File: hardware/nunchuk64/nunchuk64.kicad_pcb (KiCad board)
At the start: 2 copper layers, 49.9 x 41.5 mm, 28 parts, among them J1 DB9_Female, J2 DB9_Female, J3 Conn_02x03_Odd_Even, P1 CONN_WII, P2 CONN_WII, Q1 BSS138, Q2 BSS138, Q3 BSS138, Q4 BSS138, SW1 SW_Push, U1 AMS1117-3V3, U2 ATMEGA328P-AU

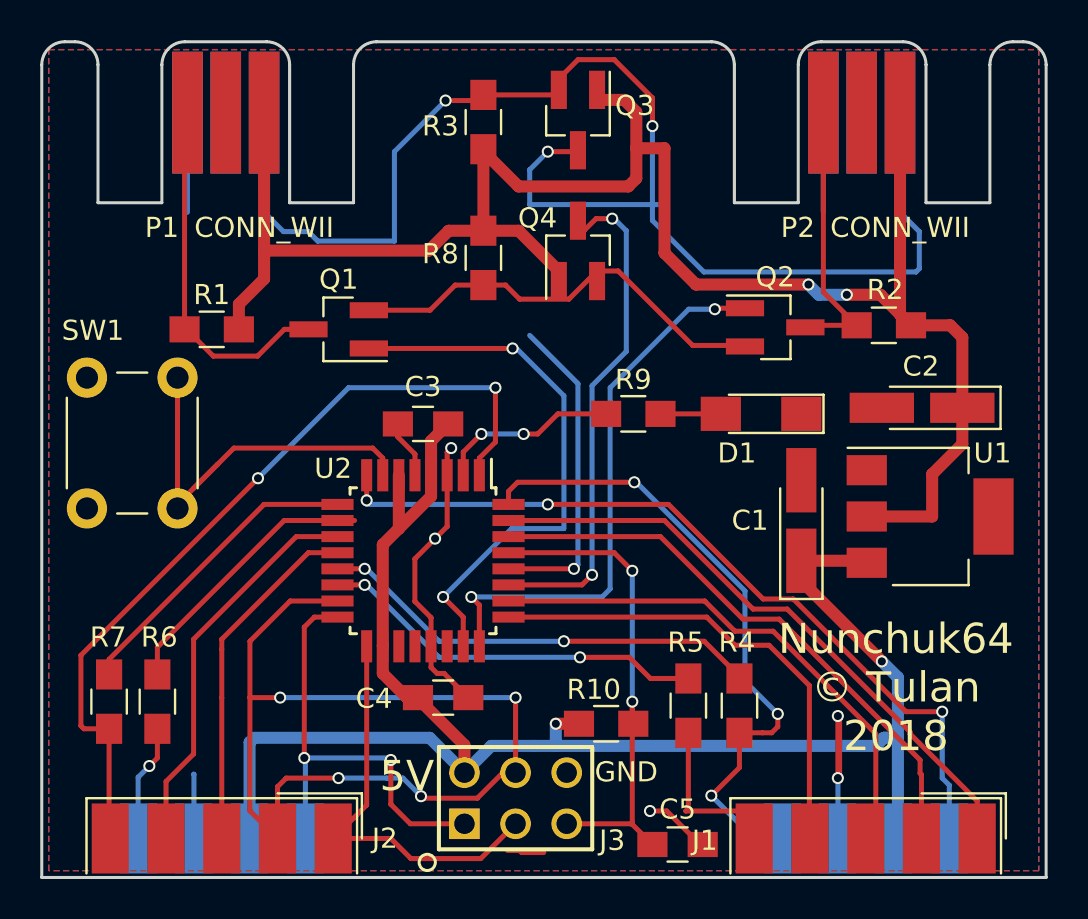
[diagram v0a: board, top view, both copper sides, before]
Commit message: fix: accidentally rotated a net. island gnd fill
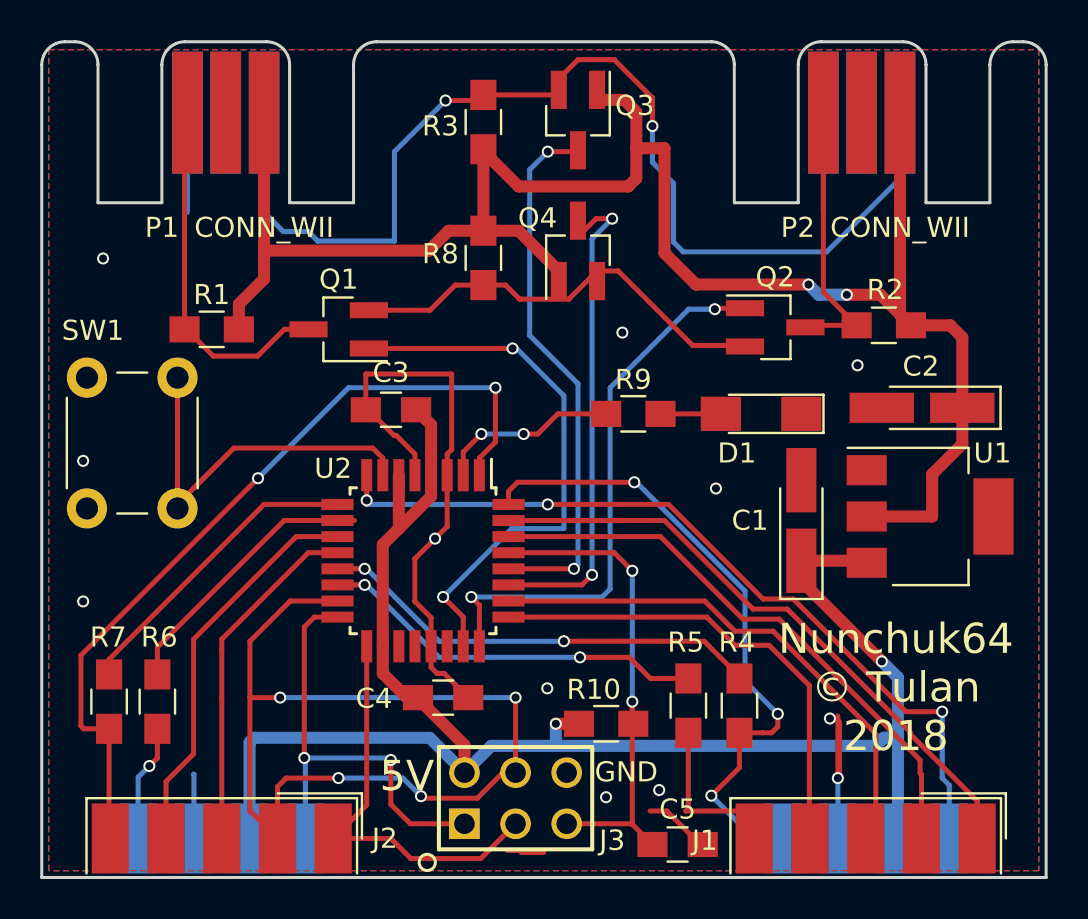
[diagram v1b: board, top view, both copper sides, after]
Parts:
- moved C3 1.74 mm to (93.8, 90.3)
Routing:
- net GND: track 42.9 -> 54.1 mm, vias 5 -> 2
- net /SCL: track 61.9 -> 57.1 mm
- net +5V: track 84.7 -> 85.4 mm
- net /SDA_: track 25.1 -> 24.4 mm
- net (no net): vias 0 -> 10

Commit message: DRC OK
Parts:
- moved C1 0.11 mm to (114.2, 95.7)
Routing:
- net GND: track 54.1 -> 112.5 mm, vias 2 -> 9
- net /SCL: track 57.1 -> 59.8 mm
- net /SDA: track 22.1 -> 22.7 mm
- net (no net): vias 10 -> 0
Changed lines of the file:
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@@
   (general
     (links 79)
-    (no_connects 2)
+    (no_connects 0)
     (area 69.224999 71.755 133.575001 129.535)
     (thickness 1.6)
     (drawings 38)
-    (tracks 412)
+    (tracks 440)
     (zones 0)
     (modules 28)
@@
     (tags "resistor 0805")
     (attr smd)
-    (fp_text reference R10 (at -0.614 -1.7) (layer F.SilkS)
-      (effects (font (size 1 1) (thickness 0.15)))
+    (fp_text reference R10 (at -0.614 -1.7) (layer B.SilkS)
+      (effects (font (size 1 1) (thickness 0.15)) (justify mirror))
     )
     (fp_text value 10k (at 0 1.75) (layer F.Fab)
@@
   )
   (module Capacitors_Tantalum_SMD:CP_Tantalum_Case-A_EIA-3216-18_Hand (layer F.Cu)
-    (at 114.2 95.8 90)
+    (at 114.1984 95.6884 90)
     (descr "Tantalum capacitor, Case A, EIA 3216-18, 3.2x1.6x1.6mm, Hand soldering footprint")
     (tags "capacitor tantalum smd")
@@
   (segment (start 100.2 112.2) (end 100.3 112.3) (width 0.25) (layer F.Cu) (net 0))
   (segment (start 99.6 112.2) (end 100.2 112.2) (width 0.25) (layer F.Cu) (net 0))
-  (via (at 101.5746 104.14) (size 0.6) (drill 0.4) (layers F.Cu B.Cu) (net 0))
-  (via (at 78.5114 99.822) (size 0.6) (drill 0.4) (layers F.Cu B.Cu) (net 0))
-  (via (at 78.5114 92.837) (size 0.6) (drill 0.4) (layers F.Cu B.Cu) (net 0))
-  (via (at 79.502 82.7786) (size 0.6) (drill 0.4) (layers F.Cu B.Cu) (net 0))
-  (via (at 104.4956 109.5502) (size 0.6) (drill 0.4) (layers F.Cu B.Cu) (net 0))
-  (via (at 116.9924 88.0872) (size 0.6) (drill 0.4) (layers F.Cu B.Cu) (net 0))
-  (via (at 109.9566 94.2086) (size 0.6) (drill 0.4) (layers F.Cu B.Cu) (net 0))
-  (via (at 105.3084 86.4616) (size 0.6) (drill 0.4) (layers F.Cu B.Cu) (net 0))
-  (via (at 107.1372 109.1946) (size 0.6) (drill 0.4) (layers F.Cu B.Cu) (net 0))
-  (via (at 115.6208 105.6386) (size 0.6) (drill 0.4) (layers F.Cu B.Cu) (net 0))
   (segment (start 122.94 111.6) (end 122.94 109.74) (width 0.25) (layer F.Cu) (net 1))
   (segment (start 122.94 109.74) (end 119.6 106.4) (width 0.25) (layer F.Cu) (net 1))
@@
   (segment (start 94.2 96.2) (end 94.2 93.55) (width 0.6) (layer F.Cu) (net 7))
   (segment (start 93.4 102.05) (end 93.4 102.85) (width 0.25) (layer F.Cu) (net 7))
+  (segment (start 103.378 103.5812) (end 99.6688 103.5812) (width 0.25) (layer F.Cu) (net 8))
+  (segment (start 99.6688 103.5812) (end 98.65 104.6) (width 0.25) (layer F.Cu) (net 8))
+  (segment (start 98.65 104.6) (end 97.65 104.6) (width 0.25) (layer F.Cu) (net 8))
+  (segment (start 103.886 104.0892) (end 103.378 103.5812) (width 0.25) (layer F.Cu) (net 8))
+  (segment (start 102.3112 104.1146) (end 103.8606 104.1146) (width 0.25) (layer B.Cu) (net 8))
+  (segment (start 103.8606 104.1146) (end 103.886 104.0892) (width 0.25) (layer B.Cu) (net 8))
+  (via (at 103.886 104.0892) (size 0.6) (drill 0.4) (layers F.Cu B.Cu) (net 8))
+  (segment (start 100.0498 103.2002) (end 101.3968 103.2002) (width 0.25) (layer F.Cu) (net 8))
+  (segment (start 101.3968 103.2002) (end 102.3112 104.1146) (width 0.25) (layer F.Cu) (net 8))
+  (via (at 102.3112 104.1146) (size 0.6) (drill 0.4) (layers F.Cu B.Cu) (net 8))
+  (segment (start 98.65 104.6) (end 100.0498 103.2002) (width 0.25) (layer F.Cu) (net 8))
+  (segment (start 104.4448 109.1946) (end 103.4046 109.1946) (width 0.25) (layer F.Cu) (net 8))
+  (segment (start 103.4046 109.1946) (end 102.54 108.33) (width 0.25) (layer F.Cu) (net 8))
+  (segment (start 106.9848 109.1438) (end 104.4956 109.1438) (width 0.25) (layer B.Cu) (net 8))
+  (segment (start 104.4956 109.1438) (end 104.4448 109.1946) (width 0.25) (layer B.Cu) (net 8))
+  (via (at 104.4448 109.1946) (size 0.6) (drill 0.4) (layers F.Cu B.Cu) (net 8))
+  (segment (start 109.175 111.9) (end 106.9848 109.7098) (width 0.25) (layer F.Cu) (net 8))
+  (segment (start 106.9848 109.7098) (end 106.9848 109.1438) (width 0.25) (layer F.Cu) (net 8))
+  (via (at 106.9848 109.1438) (size 0.6) (drill 0.4) (layers F.Cu B.Cu) (net 8))
+  (segment (start 106.9848 88.6968) (end 117.6968 88.6968) (width 0.25) (layer F.Cu) (net 8))
+  (segment (start 117.6968 88.6968) (end 118.2 89.2) (width 0.25) (layer F.Cu) (net 8))
+  (segment (start 118.2 89.2) (end 118.2 90.2) (width 0.25) (layer F.Cu) (net 8))
+  (segment (start 108.0516 88.4936) (end 107.188 88.4936) (width 0.25) (layer B.Cu) (net 8))
+  (segment (start 107.188 88.4936) (end 106.9848 88.6968) (width 0.25) (layer B.Cu) (net 8))
+  (via (at 106.9848 88.6968) (size 0.6) (drill 0.4) (layers F.Cu B.Cu) (net 8))
+  (segment (start 113.2936 88.4936) (end 108.0516 88.4936) (width 0.25) (layer F.Cu) (net 8))
+  (via (at 108.0516 88.4936) (size 0.6) (drill 0.4) (layers F.Cu B.Cu) (net 8))
+  (segment (start 114.2 90.5) (end 114.2 89.4) (width 0.25) (layer F.Cu) (net 8))
+  (segment (start 114.2 89.4) (end 113.2936 88.4936) (width 0.25) (layer F.Cu) (net 8))
+  (segment (start 85.808736 90.8304) (end 80.8304 90.8304) (width 0.25) (layer B.Cu) (net 8))
+  (segment (start 80.8304 90.8304) (end 78.7 88.7) (width 0.25) (layer B.Cu) (net 8))
+  (segment (start 87.5284 89.535) (end 87.104136 89.535) (width 0.25) (layer B.Cu) (net 8))
+  (segment (start 87.104136 89.535) (end 85.808736 90.8304) (width 0.25) (layer B.Cu) (net 8))
+  (segment (start 92.5576 90.297) (end 88.2904 90.297) (width 0.25) (layer F.Cu) (net 8))
+  (segment (start 88.2904 90.297) (end 87.5284 89.535) (width 0.25) (layer F.Cu) (net 8))
+  (via (at 87.5284 89.535) (size 0.6) (drill 0.4) (layers F.Cu B.Cu) (net 8))
   (segment (start 92.5576 88.519) (end 92.5576 90.297) (width 0.25) (layer F.Cu) (net 8))
   (segment (start 96.8248 88.519) (end 92.5576 88.519) (width 0.25) (layer F.Cu) (net 8))
@@
   (segment (start 100.15 81.4) (end 102.15 83.4) (width 0.6) (layer F.Cu) (net 17))
   (segment (start 98.4 77.35) (end 98.4 81.4) (width 0.6) (layer F.Cu) (net 17))
-  (segment (start 107.8484 79.0448) (end 106.8 77.9964) (width 0.25) (layer B.Cu) (net 18))
+  (segment (start 107.8484 79.0448) (end 107.8484 76.6318) (width 0.25) (layer B.Cu) (net 18))
+  (segment (start 107.8484 76.6318) (end 107.3912 76.1746) (width 0.25) (layer B.Cu) (net 18))
+  (segment (start 104.902 72.898) (end 107.3912 75.3872) (width 0.25) (layer F.Cu) (net 18))
+  (segment (start 107.3912 75.3872) (end 107.3912 76.1746) (width 0.25) (layer F.Cu) (net 18))
   (segment (start 108.331 82.4484) (end 107.8484 81.9658) (width 0.25) (layer B.Cu) (net 18))
   (segment (start 107.8484 81.9658) (end 107.8484 79.0448) (width 0.25) (layer B.Cu) (net 18))
   (segment (start 115.4616 82.4484) (end 108.331 82.4484) (width 0.25) (layer B.Cu) (net 18))
   (segment (start 119.105 78.805) (end 115.4616 82.4484) (width 0.25) (layer B.Cu) (net 18))
-  (segment (start 106.8 77.9964) (end 106.8 76.2) (width 0.25) (layer B.Cu) (net 18))
   (segment (start 119.105 75.53) (end 119.105 78.805) (width 0.25) (layer B.Cu) (net 18))
   (segment (start 104.902 72.898) (end 103.102 72.898) (width 0.25) (layer F.Cu) (net 18))
@@
   (segment (start 102.15 73.85) (end 102.15 74.4) (width 0.25) (layer F.Cu) (net 18))
   (segment (start 106.8 74.796) (end 104.902 72.898) (width 0.25) (layer F.Cu) (net 18))
-  (segment (start 106.8 76.2) (end 106.8 74.796) (width 0.25) (layer F.Cu) (net 18))
-  (via (at 106.8 76.2) (size 0.6) (drill 0.4) (layers F.Cu B.Cu) (net 18))
+  (via (at 107.3912 76.1746) (size 0.6) (drill 0.4) (layers F.Cu B.Cu) (net 18))
   (segment (start 93.98 81.915) (end 93.98 77.47) (width 0.25) (layer B.Cu) (net 18))
   (segment (start 93.98 77.47) (end 96.52 74.93) (width 0.25) (layer B.Cu) (net 18))
@@
   (segment (start 116.95 86.1) (end 114 86.1) (width 0.25) (layer F.Cu) (net 29))
   (segment (start 114 86.1) (end 113.9 86.2) (width 0.25) (layer F.Cu) (net 29))
+  (segment (start 104.05 83.9) (end 104.05 84.45) (width 0.25) (layer F.Cu) (net 30))
+  (segment (start 104.05 84.45) (end 103.156 85.344) (width 0.25) (layer F.Cu) (net 30))
+  (segment (start 103.156 85.344) (end 101.387999 85.344) (width 0.25) (layer F.Cu) (net 30))
+  (segment (start 101.387999 85.344) (end 100.143999 84.1) (width 0.25) (layer F.Cu) (net 30))
+  (segment (start 100.143999 84.1) (end 98.4 84.1) (width 0.25) (layer F.Cu) (net 30))
   (segment (start 97.002 84.1) (end 95.752 85.35) (width 0.25) (layer F.Cu) (net 30))
   (segment (start 95.752 85.35) (end 92.71 85.35) (width 0.25) (layer F.Cu) (net 30))
@@
   (segment (start 108.8 87.1) (end 111.85 87.1) (width 0.25) (layer F.Cu) (net 30))
   (segment (start 111.85 87.1) (end 111.9 87.15) (width 0.25) (layer F.Cu) (net 30))
-  (segment (start 98.4 84.1) (end 99.5 84.1) (width 0.25) (layer F.Cu) (net 30))
-  (segment (start 99.5 84.1) (end 100.2 84.8) (width 0.25) (layer F.Cu) (net 30))
-  (segment (start 100.2 84.8) (end 102.65 84.8) (width 0.25) (layer F.Cu) (net 30))
-  (segment (start 102.65 84.8) (end 104.05 83.4) (width 0.25) (layer F.Cu) (net 30))
   (segment (start 107.2 90.5) (end 110.2 90.5) (width 0.25) (layer F.Cu) (net 31))
   (segment (start 101.1 91.5) (end 102.1 90.5) (width 0.25) (layer F.Cu) (net 32))
